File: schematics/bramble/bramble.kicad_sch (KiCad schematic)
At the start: 0 parts

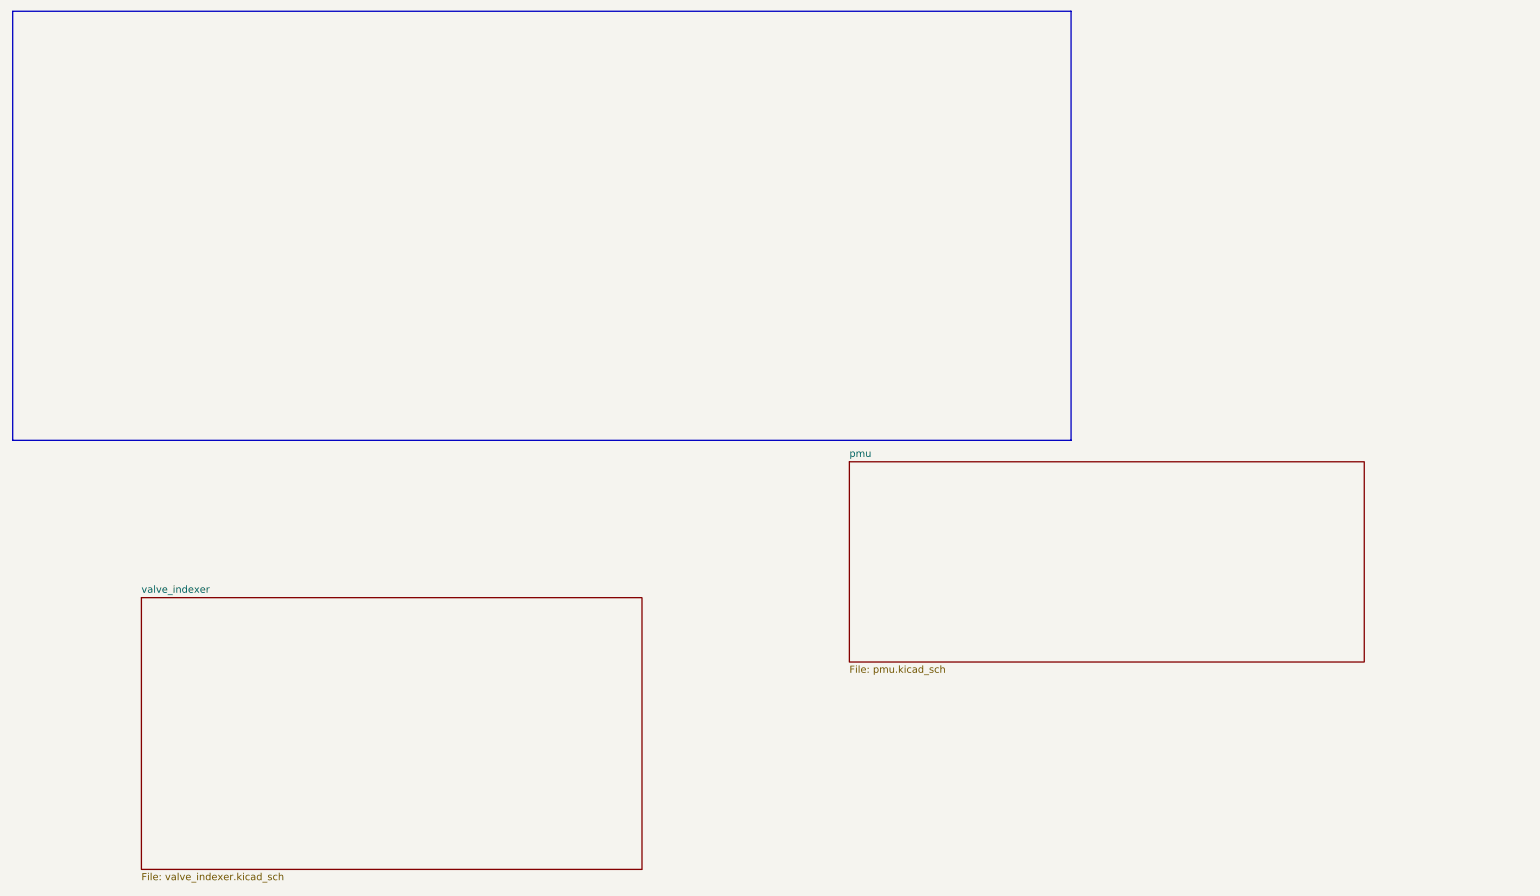
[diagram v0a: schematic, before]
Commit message: Update valve controller pin mapping for Feather RP2040
- Changed H-bridge pins to use analog-capable GPIOs:
  - MOTOR_LO_1: GPIO26 (A0)
  - MOTOR_LO_2: GPIO27 (A1)
  - MOTOR_HI_1: GPIO28 (A2)
  - MOTOR_HI_2: GPIO29 (A3)
- Updated valve count from 4 to 2 valves
- Valve control pins now on GPIO24 and GPIO25
- This avoids conflict with default I2C pins (GPIO2/3)

🤖 Generated with [Claude Code](https://claude.ai/code)

Co-Authored-By: Claude <noreply@anthropic.com>
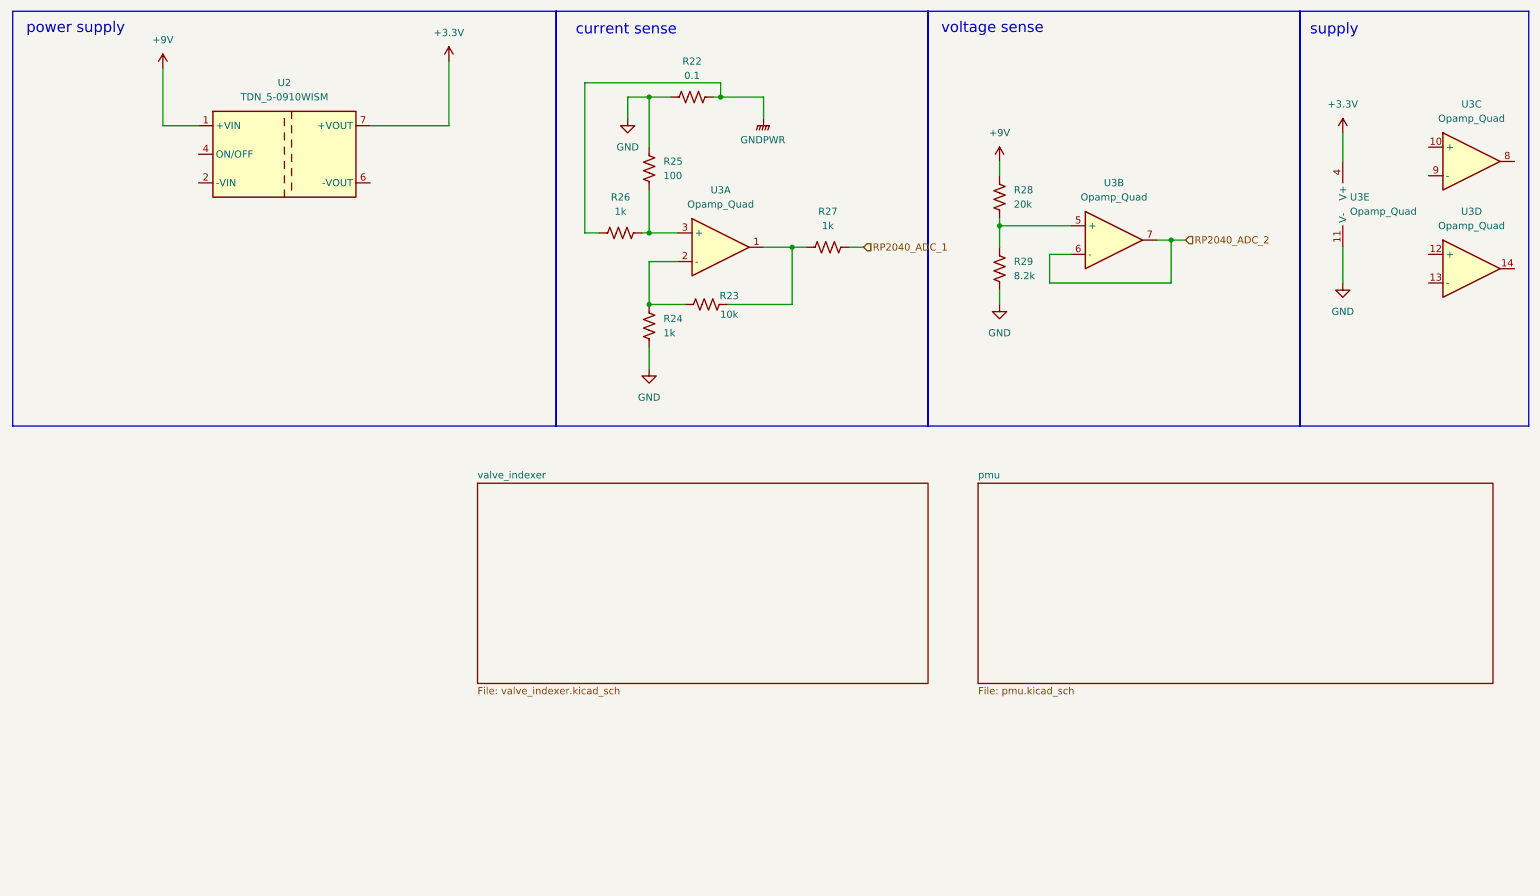
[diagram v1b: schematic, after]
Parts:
- added R22: 0.1, symbol Device:R_US
- added R23: 10k, symbol Device:R_US
- added R24, R26, R27: 1k, symbol Device:R_US
- added R25: 100, symbol Device:R_US
- added R28: 20k, symbol Device:R_US
- added R29: 8.2k, symbol Device:R_US
- added U2: TDN_5-0910WISM, Converter_DCDC:Converter_DCDC_TRACO_TDN_5-xxxxWISM_SMD, symbol Regulator_Switching:TDN_5-0910WISM
- added U3: Opamp_Quad, symbol Device:Opamp_Quad
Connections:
- new net: R23.2, R27.2, U3.1
- new net: R23.1, R24.2, U3.2 (-)
- new net: R25.1, R26.1, U3.3 (+)
- new net: R28.1, R29.2, U3.5 (+)
- new net +3.3V: U2.7 (+VOUT), U3.4 (V+)
- new net +9V: R28.2, U2.1 (+VIN)
- new net GND: R22.1, R24.1, R25.2, R29.1, U3.11 (V-)
- new net GNDPWR: R22.2, R26.2
- new net RP2040_ADC_1: R27.1
- new net RP2040_ADC_2: U3.6 (-), U3.7
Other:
- note added: "current sense"
- note added: "power supply"
- note added: "supply"
- note added: "voltage sense"
